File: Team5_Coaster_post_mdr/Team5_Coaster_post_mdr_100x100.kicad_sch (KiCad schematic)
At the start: 31 parts, among them J1 Vin, J10 GND, J11 GND, J12 GND, J13 3v3, J14 GND, J15 GND, J2 HC-05, J3 10V, J4 Batt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

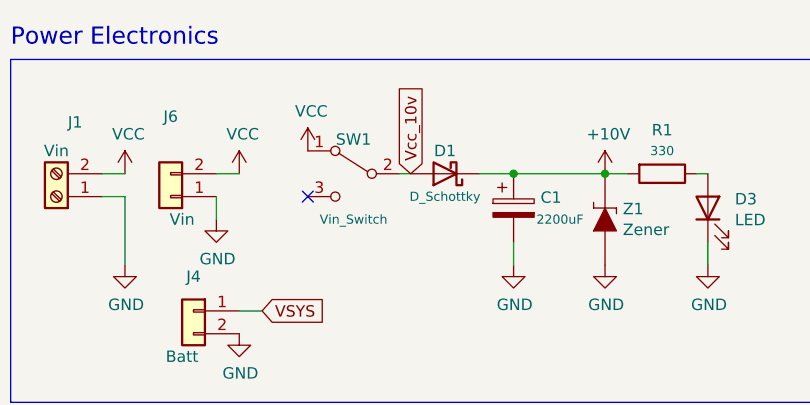
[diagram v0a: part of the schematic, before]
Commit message: Added power zone
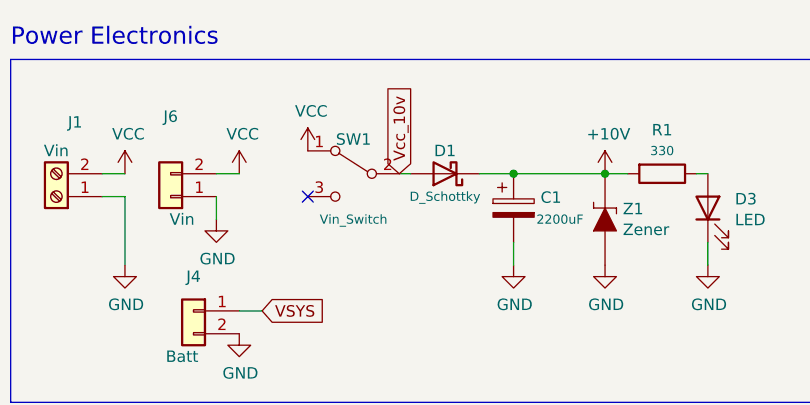
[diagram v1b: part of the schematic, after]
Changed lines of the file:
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@@
+    (stroke (width 0) (type default) (color 0 0 0 0))
+  )
+  (wire (pts (xy 69.85 38.1) (xy 68.58 38.1))
     (stroke (width 0) (type default) (color 0 0 0 0))
   )
@@
   )
   (wire (pts (xy 71.12 118.11) (xy 69.85 118.11))
-    (stroke (width 0) (type default) (color 0 0 0 0))
-  )
-  (wire (pts (xy 69.85 38.1) (xy 68.58 38.1))
     (stroke (width 0) (type default) (color 0 0 0 0))
   )
@@
     )
   )
-  (global_label "Vcc_10v" (shape input) (at 69.85 38.1 90) (fields_autoplaced)
-    (effects (font (size 1.27 1.27)) (justify left))
-    (property "Intersheet References" "${INTERSHEET_REFS}" (id 0) (at 69.7706 28.0669 90)
-      (effects (font (size 1.27 1.27)) (justify left) hide)
-    )
+  (global_label "Vcc_10v" (shape input) (at 68.58 38.1 90) (fields_autoplaced)
+    (effects (font (size 1.27 1.27)) (justify left))
+    (property "Intersheet References" "${INTERSHEET_REFS}" (id 0) (at 68.5006 28.0669 90)
+      (effects (font (size 1.27 1.27)) (justify left) hide)
+    )
